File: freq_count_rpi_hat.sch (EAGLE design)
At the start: 32 parts, among them IC1 LTC6752, IC2 LTC6752, P1 47k, U1 SN74LV8154PW, U2 SN74LV8154PW, X1 RASPI_BOARD_B+#_HD

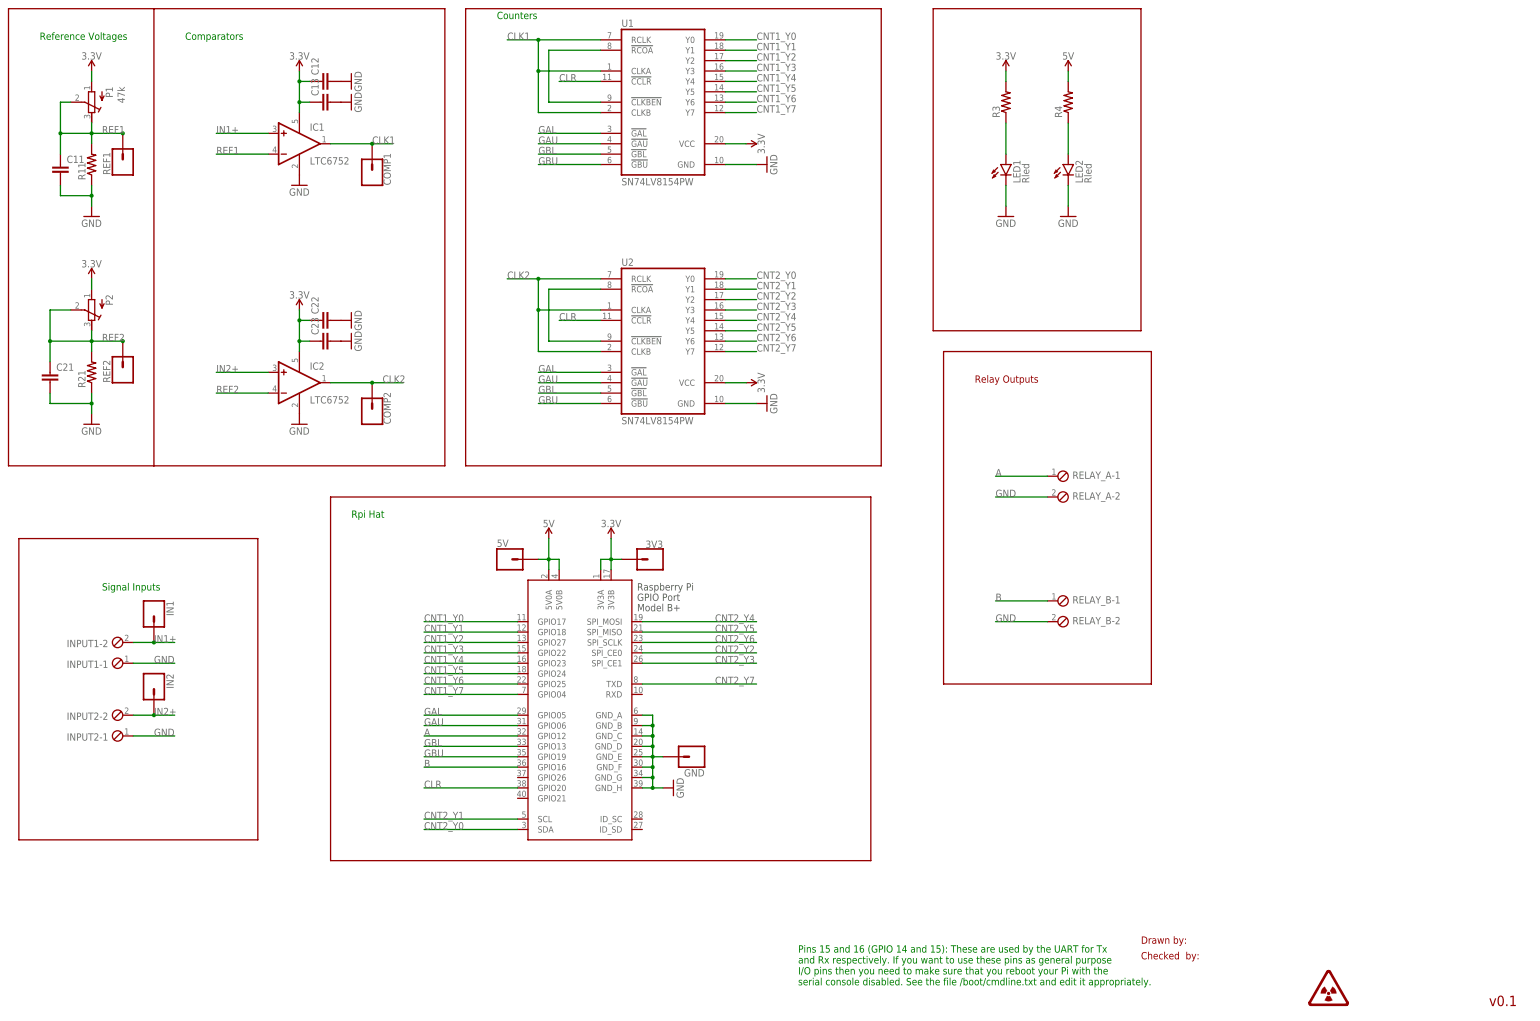
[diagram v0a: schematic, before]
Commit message: Updated with mode selection switches and mistakes in design were corrected
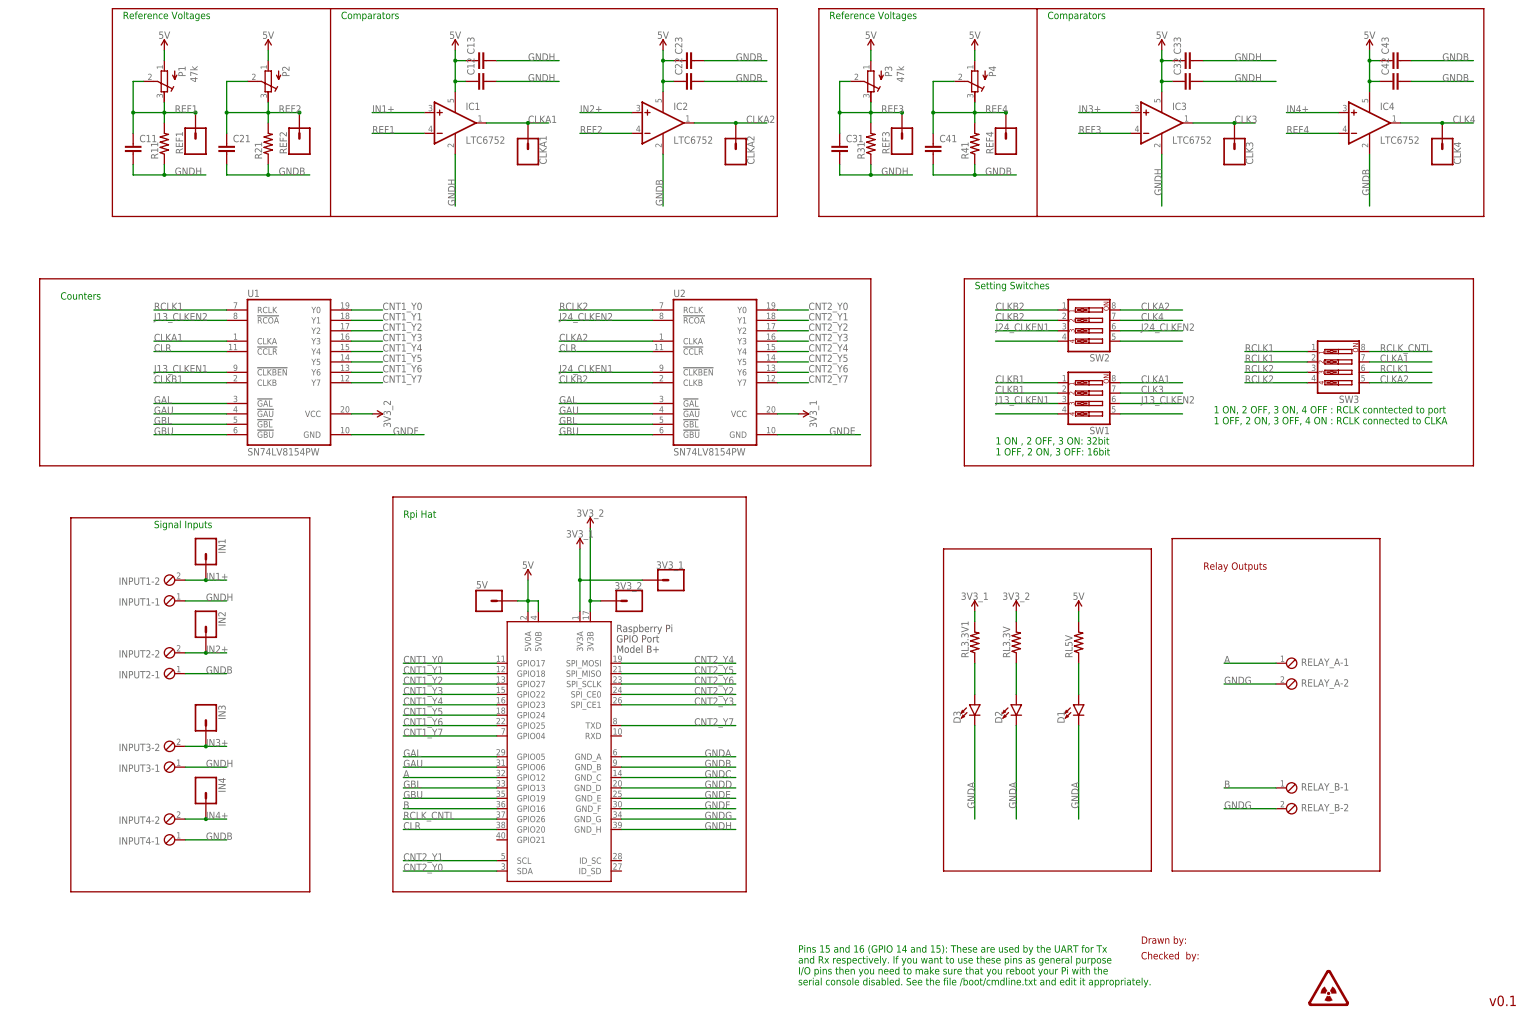
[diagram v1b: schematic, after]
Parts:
- removed 3V3, COMP1, COMP2, GND: (no value), SparkFun-Connectors:CONN_01
- removed LED1, LED2: Rled, BeagleBone_Blue_R3:LED-RED0603
- removed R3, R4: RESISTOR0805, BeagleBone_Blue_R3:RESISTOR0805
- added 3V3_1, 3V3_2, CLK3, CLK4, CLKA1, CLKA2, IN3, IN4, REF3, REF4: (no value), SparkFun-Connectors:CONN_01
- added C31, C32, C33, C41, C42, C43: (no value), resistor:C-EUC1206
- added D1, D2, D3: (no value), SparkFun-LED:LED1206
- added IC3, IC4: LTC6752, linear:OPA344N-SOT23
- added INPUT3, INPUT4: (no value), con-phoenix-254:MPT2
- added P3: 47k, rcl:R-TRIMM3296W
- added P4: (no value), rcl:R-TRIMM3296W
- added R31, R41, RL3.3V, RL3.3V1, RL5V: (no value), resistor:R-US_R1206
- added SW1, SW2, SW3: (no value), special:SW_DIP-4
- C11, C12, C13, C21, C22, C23: value CAPACITOR-N0805 -> (none); device BeagleBone_Blue_R3:CAPACITOR-N0805 -> resistor:C-EUC1206
- R11: value 470R -> (none); device BeagleBone_Blue_R3:RESISTOR0805 -> resistor:R-US_R1206
- R21: value RESISTOR0805 -> (none); device BeagleBone_Blue_R3:RESISTOR0805 -> resistor:R-US_R1206
- X1: value RASPI_BOARD_B+#_HD -> RASPI_BOARD_B+#_H; device raspberrypi_bastelstube_v13:RASPI_BOARD_B+#_HD -> raspberrypi_bastelstube_v13:RASPI_BOARD_B+#_H
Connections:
- removed net 3.3V: 3V3.1, C12.1, C13.1, C22.1, C23.1, IC1.V+, IC2.V+, P1.A, P2.A, R3.2, U1.VCC, U2.VCC, X1.3V3A, X1.3V3B
- removed net CLK1: COMP1.1, IC1.OUT, U1.CLKA, U1.CLKB, U1.RCLK
- removed net CLK2: COMP2.1, IC2.OUT, U2.CLKA, U2.CLKB, U2.RCLK
- removed net GND: C11.2, C12.2, C13.2, C21.2, C22.2, C23.2, GND.1, IC1.V-, IC2.V-, INPUT1-1.1, INPUT2-1.1, LED1.C, LED2.C, R11.1, R21.1, RELAY_A-2.1, RELAY_B-2.1, U1.GND, U2.GND, X1.GND_A, X1.GND_B, X1.GND_C, X1.GND_D, X1.GND_E, X1.GND_F, X1.GND_G, X1.GND_H
- removed net N$21: U1.!CLKBEN!, U1.!RCOA!
- removed net N$22: U2.!CLKBEN!, U2.!RCOA!
- new net CLK3: CLK3.1, IC3.OUT, SW1.7
- new net CLK4: CLK4.1, IC4.OUT, SW2.7
- new net CLKA1: CLKA1.1, IC1.OUT, SW1.8, SW3.7, U1.CLKA
- new net CLKA2: CLKA2.1, IC2.OUT, SW2.8, SW3.5, U2.CLKA
- new net CLKB1: SW1.1, SW1.2, U1.CLKB
- new net CLKB2: SW2.1, SW2.2, U2.CLKB
- new net GNDA: D1.C, D2.C, D3.C, X1.GND_A
- new net GNDB: C21.2, C22.2, C23.2, C41.2, C42.2, C43.2, IC2.V-, IC4.V-, INPUT2-1.1, INPUT4-1.1, R21.1, R41.1, X1.GND_B
- new net GNDC: X1.GND_C
- new net GNDD: X1.GND_D
- new net GNDE: U2.GND, X1.GND_E
- new net GNDF: U1.GND, X1.GND_F
- new net GNDG: RELAY_A-2.1, RELAY_B-2.1, X1.GND_G
- new net GNDH: C11.2, C12.2, C13.2, C31.2, C32.2, C33.2, IC1.V-, IC3.V-, INPUT1-1.1, INPUT3-1.1, R11.1, R31.1, X1.GND_H
- new net IN3+: IC3.+IN, IN3.1, INPUT3-2.1
- new net IN4+: IC4.+IN, IN4.1, INPUT4-2.1
- new net J13_CLKEN1: SW1.3, U1.!CLKBEN!
- new net J13_CLKEN2: SW1.6, U1.!RCOA!
- new net J24_CLKEN1: SW2.3, U2.!CLKBEN!
- new net J24_CLKEN2: SW2.6, U2.!RCOA!
- new net N$11: SW1.5
- new net N$3: D3.A, RL3.3V1.1
- new net N$4: SW1.4
- new net N$5: SW2.4
- new net N$9: SW2.5
- new net RCLK1: SW3.1, SW3.2, SW3.6, U1.RCLK
- new net RCLK2: SW3.3, SW3.4, U2.RCLK
- new net RCLK_CNTL: SW3.8, X1.GPIO26
- new net REF3: C31.1, IC3.-IN, P3.E, P3.S, R31.2, REF3.1
- new net REF4: C41.1, IC4.-IN, P4.E, P4.S, R41.2, REF4.1
- new net VCC_1: 3V3_1.1, RL3.3V1.2, U2.VCC, X1.3V3A
- new net VCC_2: 3V3_2.1, RL3.3V.2, U1.VCC, X1.3V3B
- net 5V: now also C12.1, C13.1, C22.1, C23.1, C32.1, C33.1, C42.1, C43.1, IC1.V+, IC2.V+, IC3.V+, IC4.V+, P1.A, P2.A, P3.A, P4.A, RL5V.2; no longer R4.2
- net N$1: now also D1.A, RL5V.1; no longer LED2.A, R4.1
- net N$2: now also D2.A, RL3.3V.1; no longer LED1.A, R3.1
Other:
- note added: "1 ON , 2 OFF, 3 ON: 32bit 1 OFF, 2 ON, 3 OFF: 16bit"
- note added: "1 ON, 2 OFF, 3 ON, 4 OFF : RCLK conntected to port 1 OFF, 2 ON, 3 OFF, 4 ON : RCLK connected to CLKA"
- note added: "Setting Switches"
- moved on the sheet: 5V, C11, C12, C13, C21, C22, C23, IC1, IC2, IN1, IN2, INPUT1-1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
